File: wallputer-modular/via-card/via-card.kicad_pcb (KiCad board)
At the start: 2 copper layers, 99.7 x 99.7 mm, 1 part

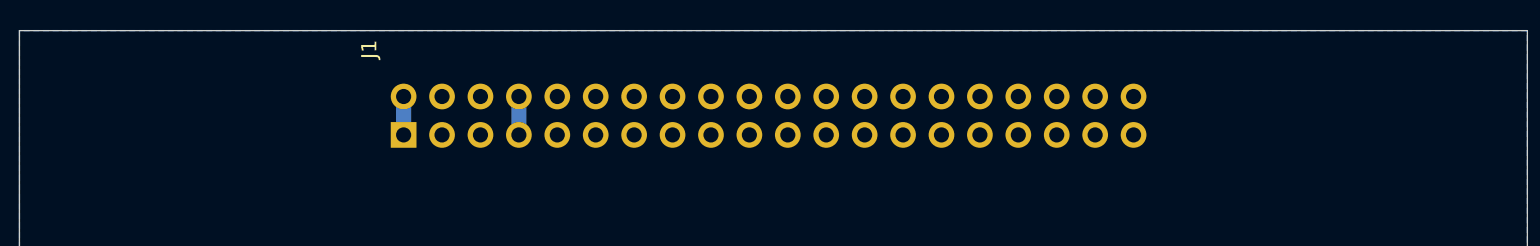
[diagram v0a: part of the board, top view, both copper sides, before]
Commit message: add card name
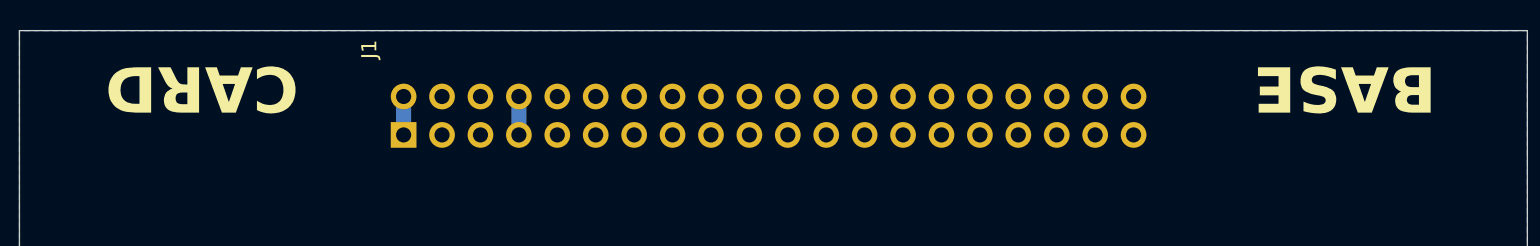
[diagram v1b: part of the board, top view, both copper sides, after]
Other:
- board text added: "BASE"
- board text added: "CARD"
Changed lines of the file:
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@@
 		(layer "Edge.Cuts")
+	)
+	(gr_text "BASE"
+		(at 151.13 67.31 180)
+		(layer "F.SilkS")
+		(effects
+			(font
+				(size 3 3)
+				(thickness 0.5)
+				(bold yes)
+			)
+		)
+	)
+	(gr_text "CARD\n"
+		(at 75.565 67.31 180)
+		(layer "F.SilkS")
+		(effects
+			(font
+				(size 3 3)
+				(thickness 0.5)
+				(bold yes)
+			)
+		)
 	)
 	(segment

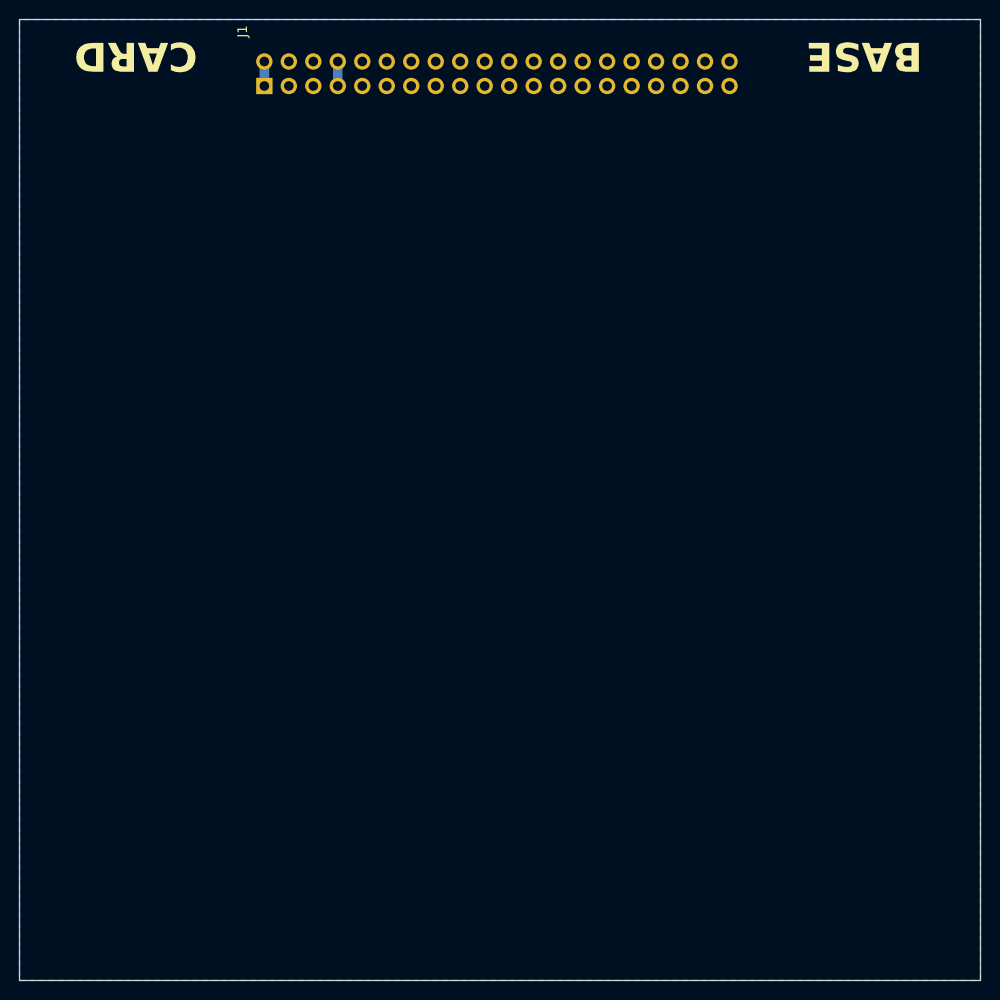
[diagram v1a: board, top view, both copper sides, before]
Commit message: implement via board
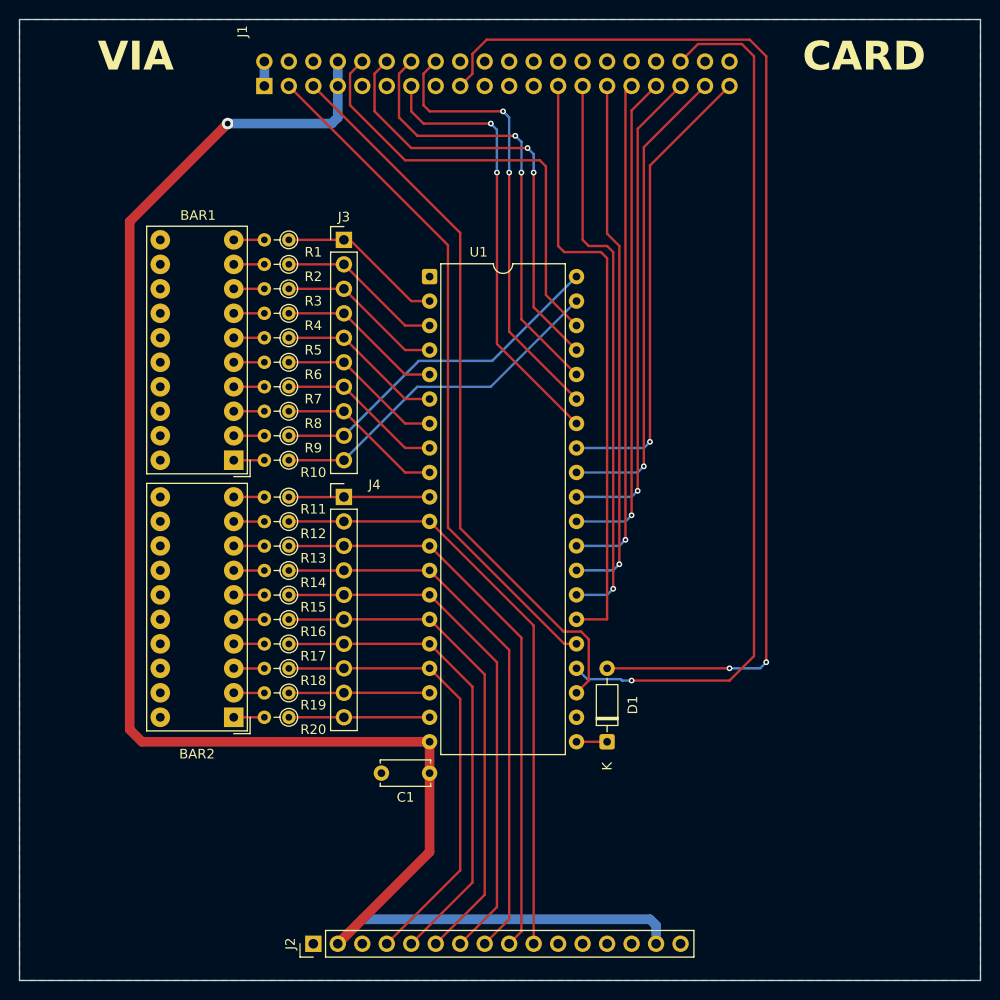
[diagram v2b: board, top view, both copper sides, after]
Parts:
- added BAR1: HDSP-4850_2, Display:HDSP-4850, F.Cu at (85.7, 109.2)
- added BAR2: HDSP-4850_2, Display:HDSP-4850, F.Cu at (85.7, 135.9)
- added C1: 100nF, Capacitor_THT:C_Disc_D5.0mm_W2.5mm_P5.00mm, F.Cu at (106.0, 141.7)
- added D1: 1N4148, Diode_THT:D_DO-35_SOD27_P7.62mm_Horizontal, F.Cu at (124.5, 138.4)
- added J2: 4x20 character display, Connector_PinHeader_2.54mm:PinHeader_1x16_P2.54mm_Vertical, F.Cu at (94.0, 159.4)
- added J3: PortA, Connector_PinHeader_2.54mm:PinHeader_1x10_P2.54mm_Vertical, F.Cu at (97.2, 86.4)
- added J4: PortB, Connector_PinHeader_2.54mm:PinHeader_1x10_P2.54mm_Vertical, F.Cu at (97.2, 113.0)
- added R1: 1k, Resistor_THT:R_Axial_DIN0204_L3.6mm_D1.6mm_P2.54mm_Vertical, F.Cu at (91.4, 86.4)
- added R10: 1k, Resistor_THT:R_Axial_DIN0204_L3.6mm_D1.6mm_P2.54mm_Vertical, F.Cu at (91.4, 109.2)
- added R11: 1k, Resistor_THT:R_Axial_DIN0204_L3.6mm_D1.6mm_P2.54mm_Vertical, F.Cu at (91.4, 113.0)
- added R12: 1k, Resistor_THT:R_Axial_DIN0204_L3.6mm_D1.6mm_P2.54mm_Vertical, F.Cu at (91.4, 115.6)
- added R13: 1k, Resistor_THT:R_Axial_DIN0204_L3.6mm_D1.6mm_P2.54mm_Vertical, F.Cu at (91.4, 118.1)
- added R14: 1k, Resistor_THT:R_Axial_DIN0204_L3.6mm_D1.6mm_P2.54mm_Vertical, F.Cu at (91.4, 120.7)
- added R15: 1k, Resistor_THT:R_Axial_DIN0204_L3.6mm_D1.6mm_P2.54mm_Vertical, F.Cu at (91.4, 123.2)
- added R16: 1k, Resistor_THT:R_Axial_DIN0204_L3.6mm_D1.6mm_P2.54mm_Vertical, F.Cu at (91.4, 125.7)
- added R17: 1k, Resistor_THT:R_Axial_DIN0204_L3.6mm_D1.6mm_P2.54mm_Vertical, F.Cu at (91.4, 128.3)
- added R18: 1k, Resistor_THT:R_Axial_DIN0204_L3.6mm_D1.6mm_P2.54mm_Vertical, F.Cu at (91.4, 130.8)
- added R19: 1k, Resistor_THT:R_Axial_DIN0204_L3.6mm_D1.6mm_P2.54mm_Vertical, F.Cu at (91.4, 133.4)
- added R2: 1k, Resistor_THT:R_Axial_DIN0204_L3.6mm_D1.6mm_P2.54mm_Vertical, F.Cu at (91.4, 88.9)
- added R20: 1k, Resistor_THT:R_Axial_DIN0204_L3.6mm_D1.6mm_P2.54mm_Vertical, F.Cu at (91.4, 135.9)
- added R3: 1k, Resistor_THT:R_Axial_DIN0204_L3.6mm_D1.6mm_P2.54mm_Vertical, F.Cu at (91.4, 91.4)
- added R4: 1k, Resistor_THT:R_Axial_DIN0204_L3.6mm_D1.6mm_P2.54mm_Vertical, F.Cu at (91.4, 94.0)
- added R5: 1k, Resistor_THT:R_Axial_DIN0204_L3.6mm_D1.6mm_P2.54mm_Vertical, F.Cu at (91.4, 96.5)
- added R6: 1k, Resistor_THT:R_Axial_DIN0204_L3.6mm_D1.6mm_P2.54mm_Vertical, F.Cu at (91.4, 99.1)
- added R7: 1k, Resistor_THT:R_Axial_DIN0204_L3.6mm_D1.6mm_P2.54mm_Vertical, F.Cu at (91.4, 101.6)
- added R8: 1k, Resistor_THT:R_Axial_DIN0204_L3.6mm_D1.6mm_P2.54mm_Vertical, F.Cu at (91.4, 104.1)
- added R9: 1k, Resistor_THT:R_Axial_DIN0204_L3.6mm_D1.6mm_P2.54mm_Vertical, F.Cu at (91.4, 106.7)
- added U1: W65C22SxP, Package_DIP:DIP-40_W15.24mm, F.Cu at (106.0, 90.2)
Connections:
- J1 pad 10: unconnected-(J1-A5-Pad10) -> /A5
- J1 pad 11: unconnected-(J1-A6-Pad11) -> /A6
- J1 pad 12: unconnected-(J1-A7-Pad12) -> /A7
- J1 pad 13: unconnected-(J1-A8-Pad13) -> /A8
- J1 pad 14: unconnected-(J1-A9-Pad14) -> /A9
- J1 pad 15: unconnected-(J1-A10-Pad15) -> /A10
- J1 pad 16: unconnected-(J1-A11-Pad16) -> /A11
- J1 pad 17: unconnected-(J1-A12-Pad17) -> /A12
- J1 pad 18: unconnected-(J1-A13-Pad18) -> /A13
- J1 pad 19: unconnected-(J1-A14-Pad19) -> /A14
- J1 pad 20: unconnected-(J1-A15-Pad20) -> /A15
- J1 pad 21: unconnected-(J1-D0-Pad21) -> /D0
- J1 pad 22: unconnected-(J1-D1-Pad22) -> /D1
- J1 pad 23: unconnected-(J1-D2-Pad23) -> /D2
- J1 pad 24: unconnected-(J1-D3-Pad24) -> /D3
- J1 pad 25: unconnected-(J1-D4-Pad25) -> /D4
- J1 pad 26: unconnected-(J1-D5-Pad26) -> /D5
- J1 pad 27: unconnected-(J1-D6-Pad27) -> /D6
- J1 pad 28: unconnected-(J1-D7-Pad28) -> /D7
- J1 pad 32: unconnected-(J1-IRQ/-Pad32) -> IRQ/
- J1 pad 34: unconnected-(J1-RES/-Pad34) -> RES/
- J1 pad 38: unconnected-(J1-ACC/-Pad38) -> ACC/
- J1 pad 39: unconnected-(J1-CLK-Pad39) -> CLK
- J1 pad 5: unconnected-(J1-A0-Pad5) -> /A0
- J1 pad 6: unconnected-(J1-A1-Pad6) -> /A1
- J1 pad 7: unconnected-(J1-A2-Pad7) -> /A2
- J1 pad 8: unconnected-(J1-A3-Pad8) -> /A3
- J1 pad 9: unconnected-(J1-A4-Pad9) -> /A4
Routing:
- net +5V: track 2.54 -> 177.4 mm, vias 0 -> 1
- net IRQ/: track 0.00 -> 115.3 mm, vias 0 -> 2
- net /A13: track 0.00 -> 91.1 mm, vias 0 -> 1
- net ACC/: track 0.00 -> 76.4 mm
- net CLK: track 0.00 -> 71.0 mm
- net Net-(J2-Pin_10): track 0.00 -> 62.9 mm
- net /D7: track 0.00 -> 62.8 mm
- net Net-(J2-Pin_9): track 0.00 -> 60.4 mm
- net /D6: track 0.00 -> 58.7 mm, vias 0 -> 1
- net Net-(J2-Pin_8): track 0.00 -> 57.8 mm
- net Net-(J2-Pin_7): track 0.00 -> 55.3 mm
- net /D5: track 0.00 -> 54.9 mm, vias 0 -> 1
- net Net-(J2-Pin_6): track 0.00 -> 52.7 mm
- net /D4: track 0.00 -> 52.7 mm, vias 0 -> 1
- net /D3: track 0.00 -> 51.6 mm, vias 0 -> 1
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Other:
- board text added: "VIA"
- board text removed: "BASE"
